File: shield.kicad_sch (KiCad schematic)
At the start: 0 parts

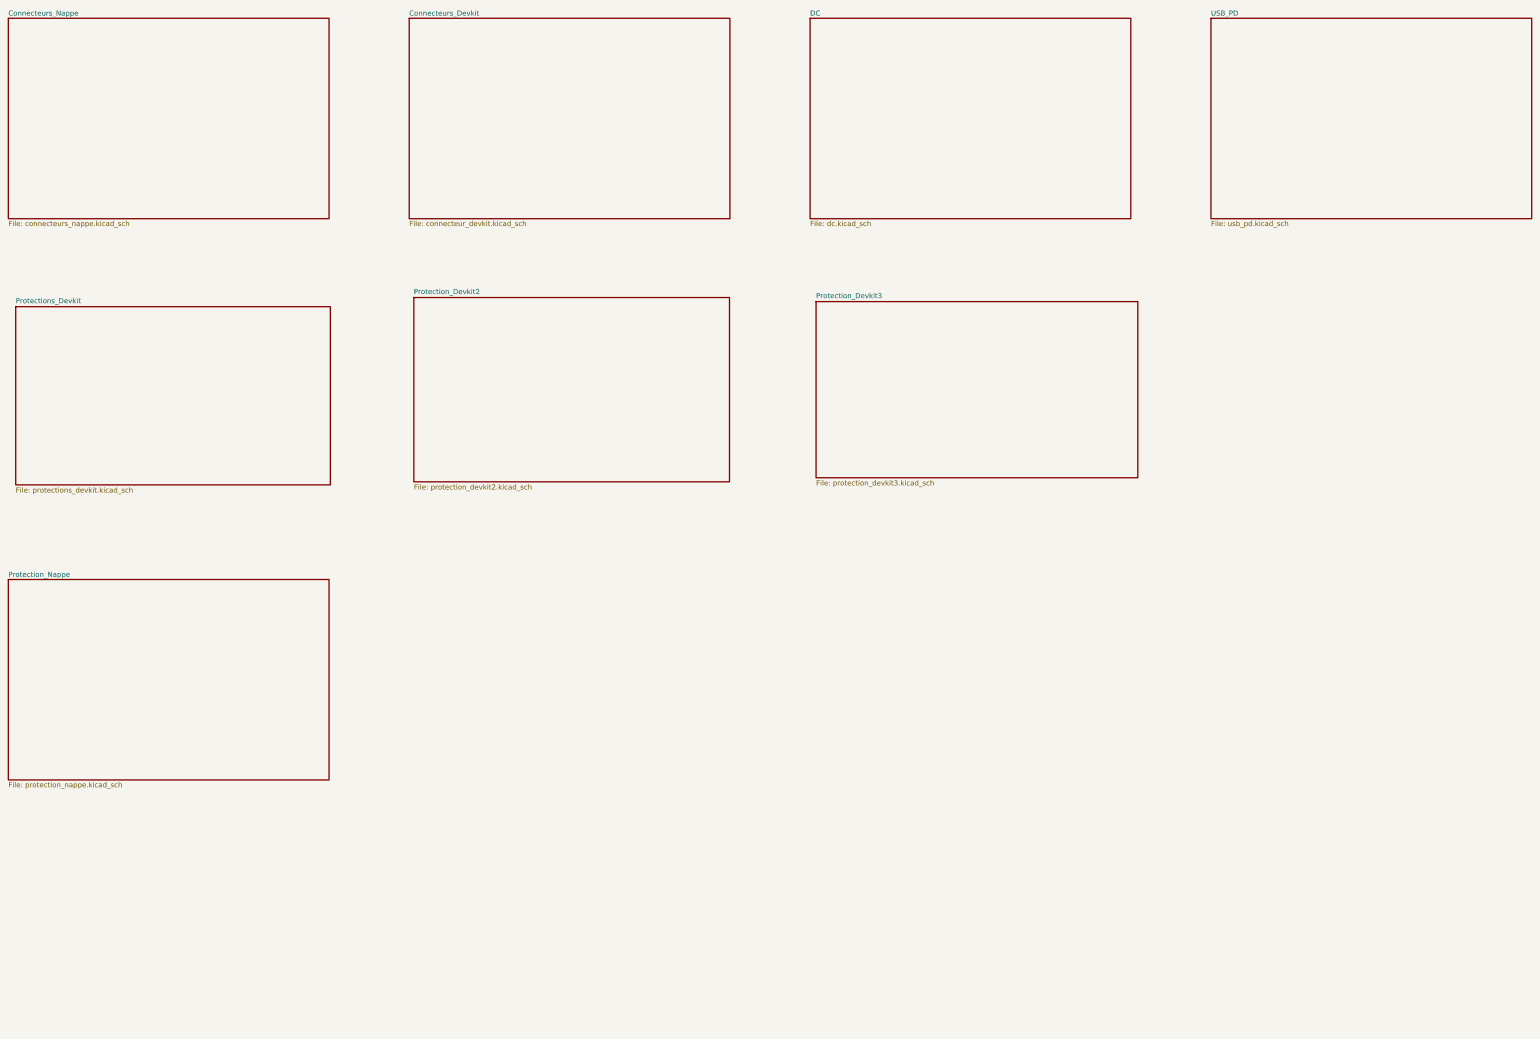
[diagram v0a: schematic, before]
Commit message: Ajoute les connecteurs dedies carte HV et carte Filament (HT)
Ecart assume a la decision #17 : ces deux premieres cartes filles ont
plus de signaux que les reserves des six nappes partagees n'en offrent
(ADC-2: 3 reserves, GPIO-1: aucune). Chaque carte recoit son propre
connecteur IDC 2x10 sur une feuille dediee, en plus des six nappes.

- connecteur_carte_hv.kicad_sch (J19/J20) : tous les signaux repris
  sont deja proteges ailleurs, aucun composant neuf.
- connecteur_ht.kicad_sch (J21) : les 5 voies ADC_8-12 du devkit,
  posees depuis le debut mais jamais cablees, sont enfin affectees
  (Vht/Temp_ht/I_Shunt_ht/I_Shunt_ht_comp/V_bias) via 5 nouveaux trios
  de protection (gabarit existant, R=22 Ohm sur le chemin comparateur
  I_Shunt_ht_comp/CMPSS3, R=100 Ohm ailleurs).
- 3 nouveaux symboles NAPPE_HV_ADC/NAPPE_HV_DIO/NAPPE_FILAMENT_HT
  (gabarit NAPPE_ADC1).
- Renommage prealable des labels ADC_8-12 en _MCU sur
  connecteur_devkit.kicad_sch (convention stricte du projet).

Verifie : check_schematic_labels.py propre sur les 3 feuilles ; ERC
feuille par feuille/categorie contre l'etat precedent, 0 violation sur
les deux nouvelles feuilles, les 5 isolated_pin_label sur ADC_8-12 ont
disparu, aucune regression ailleurs.

Hors perimetre : PCB non touche ; configuration CMPSS3 cote firmware
devkit (projet CCS separe) a faire plus tard.

Co-Authored-By: Claude Sonnet 5 <noreply@anthropic.com>
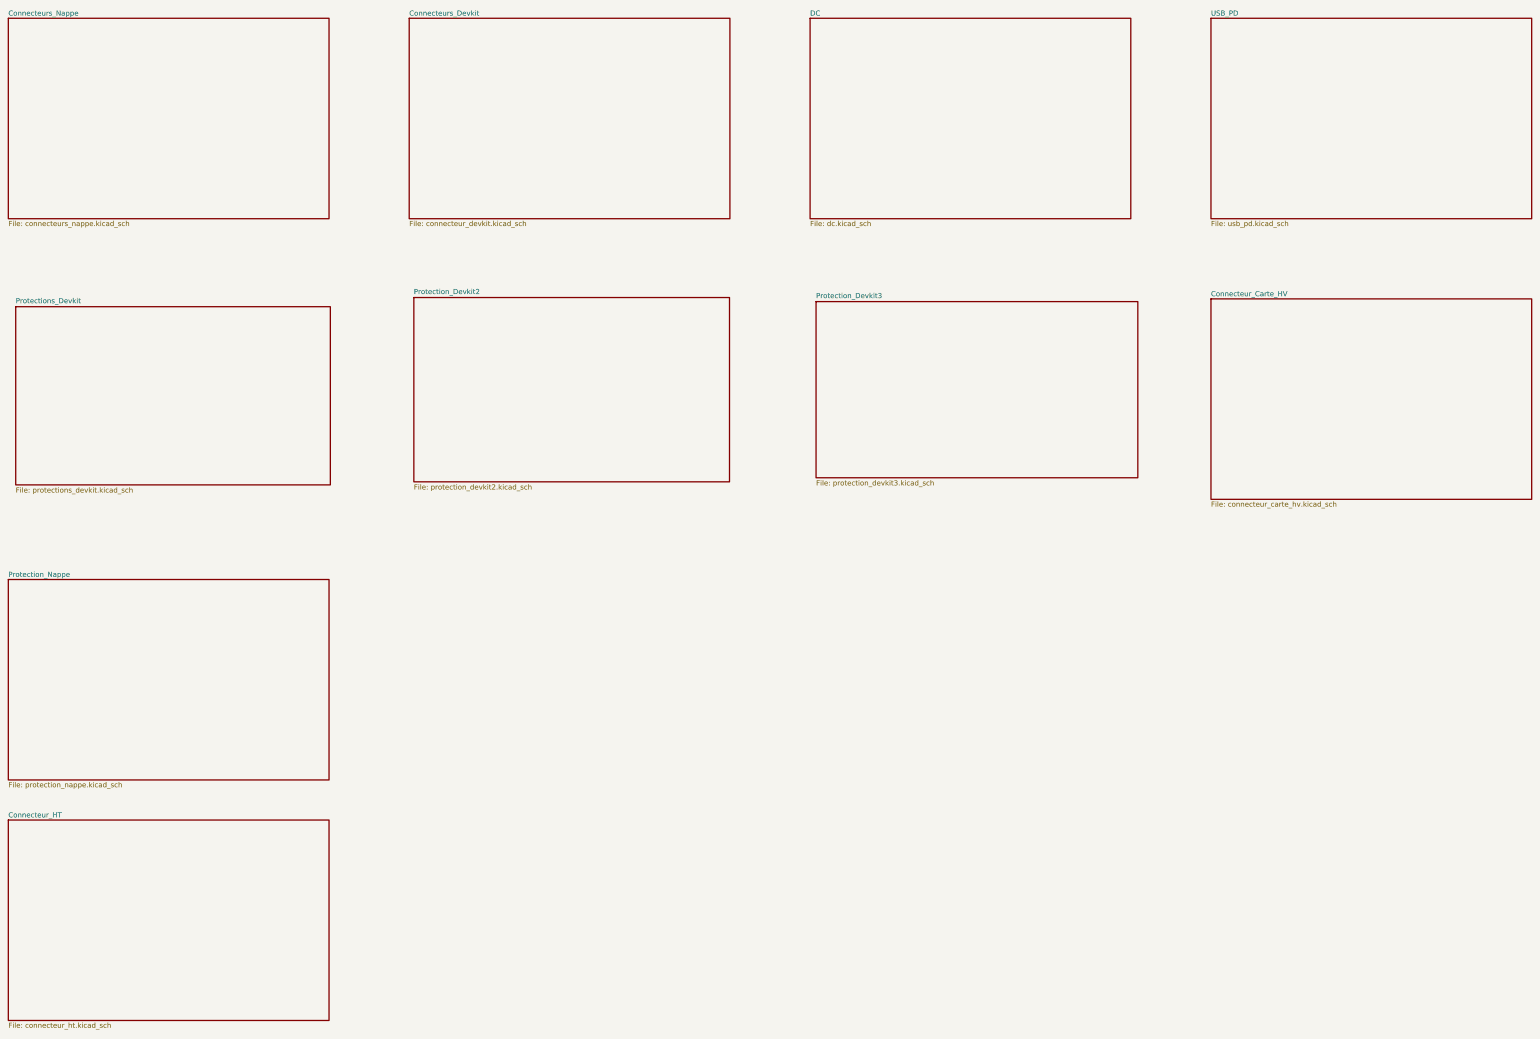
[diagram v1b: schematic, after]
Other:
- added sheet Connecteur_Carte_HV (connecteur_carte_hv.kicad_sch)
- added sheet Connecteur_HT (connecteur_ht.kicad_sch)
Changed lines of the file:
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@@
+		)
+	)
+	(sheet
+		(at 320 90)
+		(size 80 50)
+		(exclude_from_sim no)
+		(in_bom yes)
+		(on_board yes)
+		(dnp no)
+		(fields_autoplaced yes)
+		(stroke
+			(width 0.1524)
+			(type solid)
+		)
+		(fill
+			(color 0 0 0 0)
+		)
+		(property "Sheetname" "Connecteur_Carte_HV"
+			(at 320 89.5 0)
+			(show_name no)
+			(do_not_autoplace no)
+			(effects
+				(font
+					(size 1.27 1.27)
+				)
+				(justify left bottom)
+			)
+		)
+		(property "Sheetfile" "connecteur_carte_hv.kicad_sch"
+			(at 320 140.5 0)
+			(show_name no)
+			(do_not_autoplace no)
+			(effects
+				(font
+					(size 1.27 1.27)
+				)
+				(justify left top)
+			)
+		)
+		(instances
+			(project "shield"
+				(path "/3e79b37e-13ed-4a43-b954-3b2f3b716c2c"
+					(page "10")
+				)
+			)
+		)
+	)
+	(sheet
+		(at 20 220)
+		(size 80 50)
+		(exclude_from_sim no)
+		(in_bom yes)
+		(on_board yes)
+		(dnp no)
+		(fields_autoplaced yes)
+		(stroke
+			(width 0.1524)
+			(type solid)
+		)
+		(fill
+			(color 0 0 0 0)
+		)
+		(property "Sheetname" "Connecteur_HT"
+			(at 20 219.5 0)
+			(show_name no)
+			(do_not_autoplace no)
+			(effects
+				(font
+					(size 1.27 1.27)
+				)
+				(justify left bottom)
+			)
+		)
+		(property "Sheetfile" "connecteur_ht.kicad_sch"
+			(at 20 270.5 0)
+			(show_name no)
+			(do_not_autoplace no)
+			(effects
+				(font
+					(size 1.27 1.27)
+				)
+				(justify left top)
+			)
+		)
+		(instances
+			(project "shield"
+				(path "/3e79b37e-13ed-4a43-b954-3b2f3b716c2c"
+					(page "11")
+				)
+			)
 		)
 	)
